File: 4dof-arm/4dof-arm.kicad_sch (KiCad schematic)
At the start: 20 parts, among them J1 Servo-0, J2 Servo-1, J3 Servo-2, J4 Servo-3, J5 I2C, J6 I2C, J7 UART, J8 Reset, U1 bluepill-stm32f103c8, U2 NRF24L01_Breakout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

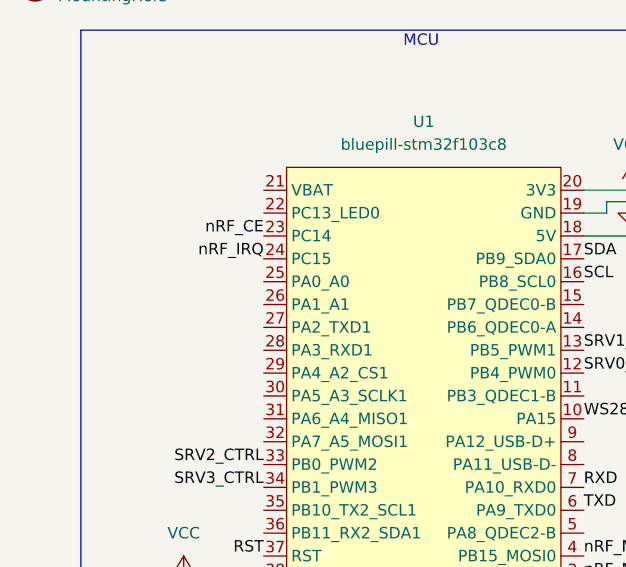
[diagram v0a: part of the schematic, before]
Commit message: 4dof-arm: Fix nRF24L01+ CE and IRQ signal
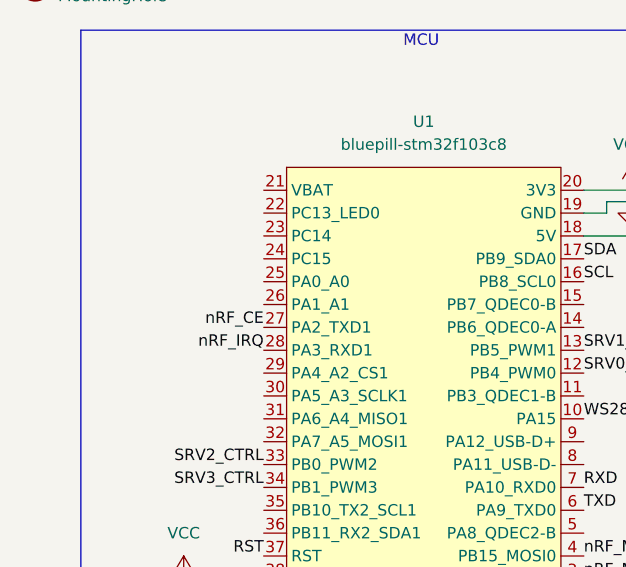
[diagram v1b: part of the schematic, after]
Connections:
- net nRF_CE: now also U1.27 (PA2_TXD1); no longer U1.23 (PC14)
- net nRF_IRQ: now also U1.28 (PA3_RXD1); no longer U1.24 (PC15)
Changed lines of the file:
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@@
     (effects (font (size 1.27 1.27)) (justify right bottom))
   )
-  (label "nRF_IRQ" (at 40.64 45.72 180) (fields_autoplaced)
+  (label "nRF_IRQ" (at 40.64 55.88 180) (fields_autoplaced)
     (effects (font (size 1.27 1.27)) (justify right bottom))
   )
-  (label "nRF_CE" (at 40.64 43.18 180) (fields_autoplaced)
+  (label "nRF_CE" (at 40.64 53.34 180) (fields_autoplaced)
     (effects (font (size 1.27 1.27)) (justify right bottom))
   )
